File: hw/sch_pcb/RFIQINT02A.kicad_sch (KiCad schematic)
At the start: 33 parts, among them J1 HEADER_2x03_PARALLEL, J2 HEADER_2x04_PARALLEL, J3 SATA7-67491-1030, J4 SATA7-67491-1030, J5 SATA7-67491-1030, J6 RJ45_RJHSE-5384, J7 RJ45_RJHSE-5384, M1 HOLE, M2 HOLE, M3 HOLE, M4 HOLE, U1 Si53322

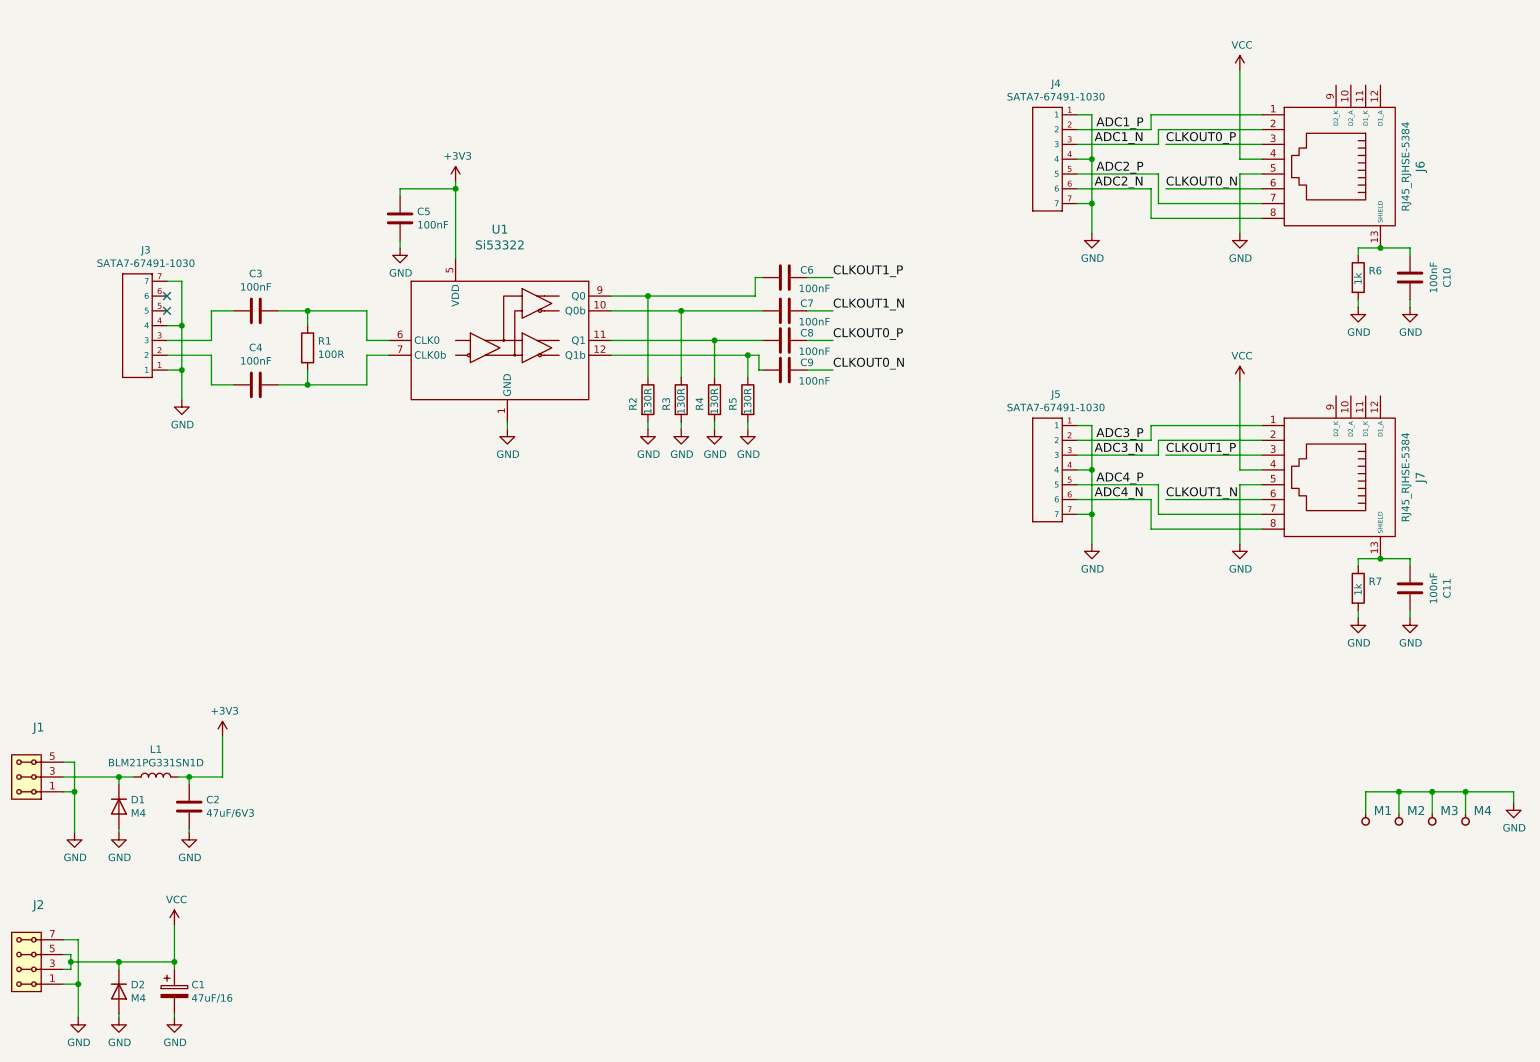
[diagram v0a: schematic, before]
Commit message: remove vias from differential pairs routing.
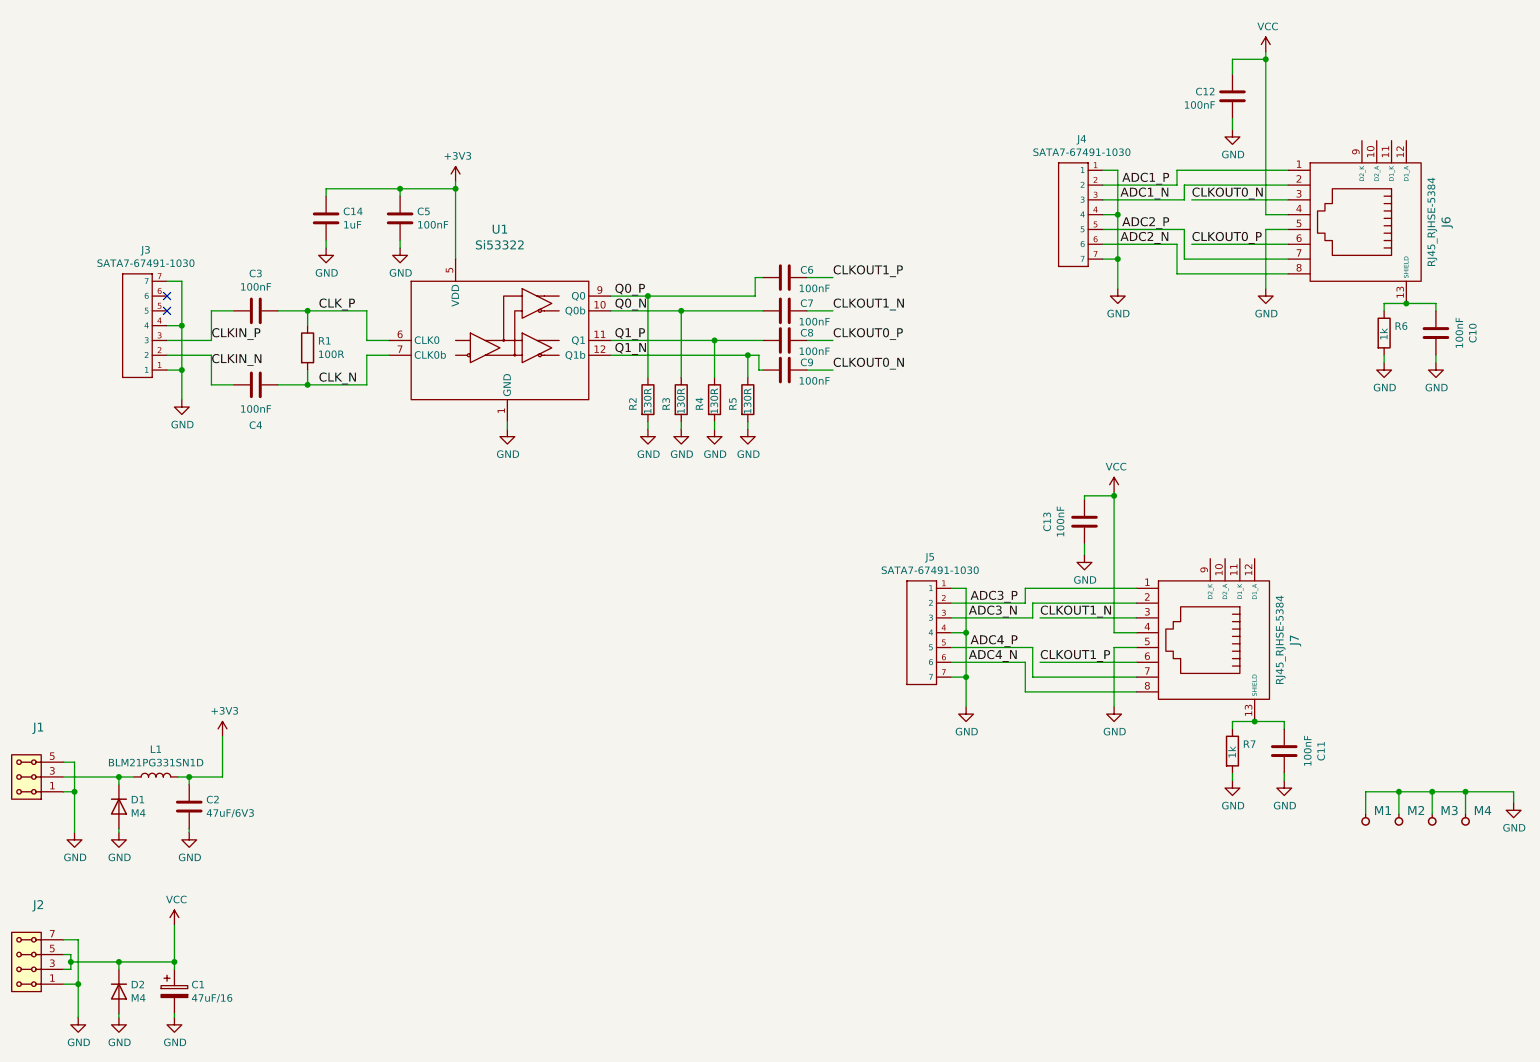
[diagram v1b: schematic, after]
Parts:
- added C12, C13: 100nF, Mlab_R:SMD-0805, symbol Device:C
- added C14: 1uF, Mlab_R:SMD-0805, symbol Device:C
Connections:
- net +3V3: now also C14.1
- net CLKOUT0_N: now also J6.3; no longer J6.6
- net CLKOUT0_P: now also J6.6; no longer J6.3
- net CLKOUT1_N: now also J7.3; no longer J7.6
- net CLKOUT1_P: now also J7.6; no longer J7.3
- net GND: now also C12.1, C13.1, C14.2
- net VCC: now also C12.2, C13.2
- net Q1_P: now reaches C8.1, R4.1, U1.11 (Q1)
- net Q0_N: now reaches C7.1, R3.1, U1.10 (Q0b)
- net Q0_P: now reaches C6.1, R2.1, U1.9 (Q0)
- net Q1_N: now reaches C9.1, R5.1, U1.12 (Q1b)
- net CLK_P: now reaches C3.2, R1.1, U1.6 (CLK0)
- net CLK_N: now reaches C4.2, R1.2, U1.7 (CLK0b)
- net CLKIN_N: now reaches C4.1, J3.2
- net CLKIN_P: now reaches C3.1, J3.3
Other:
- moved on the sheet: C10, C11, J4, J5, J6, J7, R6, R7

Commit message: Tune skew of differential pairs.
Use the RJ45 connector's LED as power indicators.
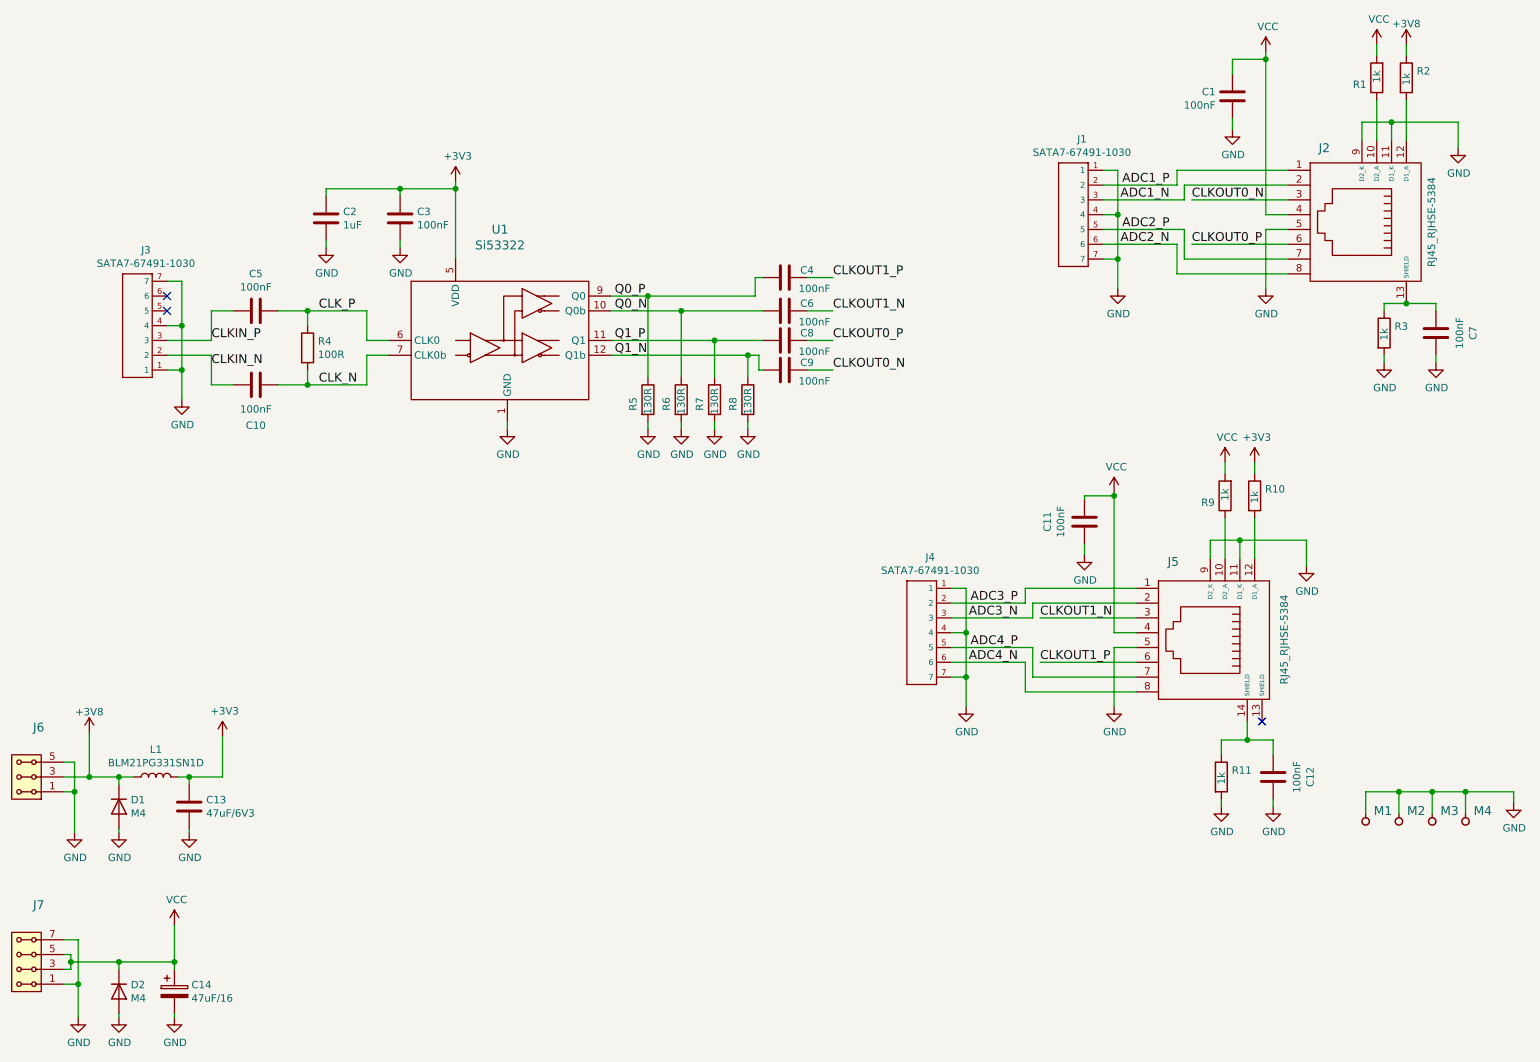
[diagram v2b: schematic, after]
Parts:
- added R1, R10, R2, R9: 1k, Mlab_R:SMD-0805, symbol Device:R
- renumbered C12 to C1, C4 to C10, C13 to C11, C11 to C12, C2 to C13, C1 to C14, C14 to C2, C5 to C3, C6 to C4, C3 to C5, C7 to C6, C10 to C7, J4 to J1, J6 to J2, J5 to J4, J7 to J5, J1 to J6, J2 to J7, R7 to R11, R6 to R3, R1 to R4, R2 to R5, R3 to R6, R4 to R7, R5 to R8
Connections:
- net +3V3: now also R10.1
- net GND: now also J2.11 (D1_K), J2.9 (D2_K), J5.11 (D1_K), J5.9 (D2_K)
- net VCC: now also R1.2, R9.2
- net at J2.10 (D2_A): now also R1.1
- net at J2.12 (D1_A): now also R2.2
- net at C12.1, R11.1: now also J5.14 (SHIELD); no longer J5.13 (SHIELD)
- net +3V8: now reaches D1.1 (K), J6.3, J6.4, L1.1
- net +3V8: now also R2.1
- net at J5.10 (D2_A): now also R9.1
- net at J5.12 (D1_A): now also R10.2
- no-connect marks 2 -> 3
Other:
- moved on the sheet: C12, R11
